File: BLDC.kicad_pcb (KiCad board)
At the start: 4 copper layers, 60 x 60 mm, 122 parts, among them J1 43650-0510, J2 436500313, J3 DNP, J4 43650-0510, U1 LMZ21700SIL, U12 MCP9808, U13 AS5047U, U17 INA250, U18 INA250, U19 INA250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

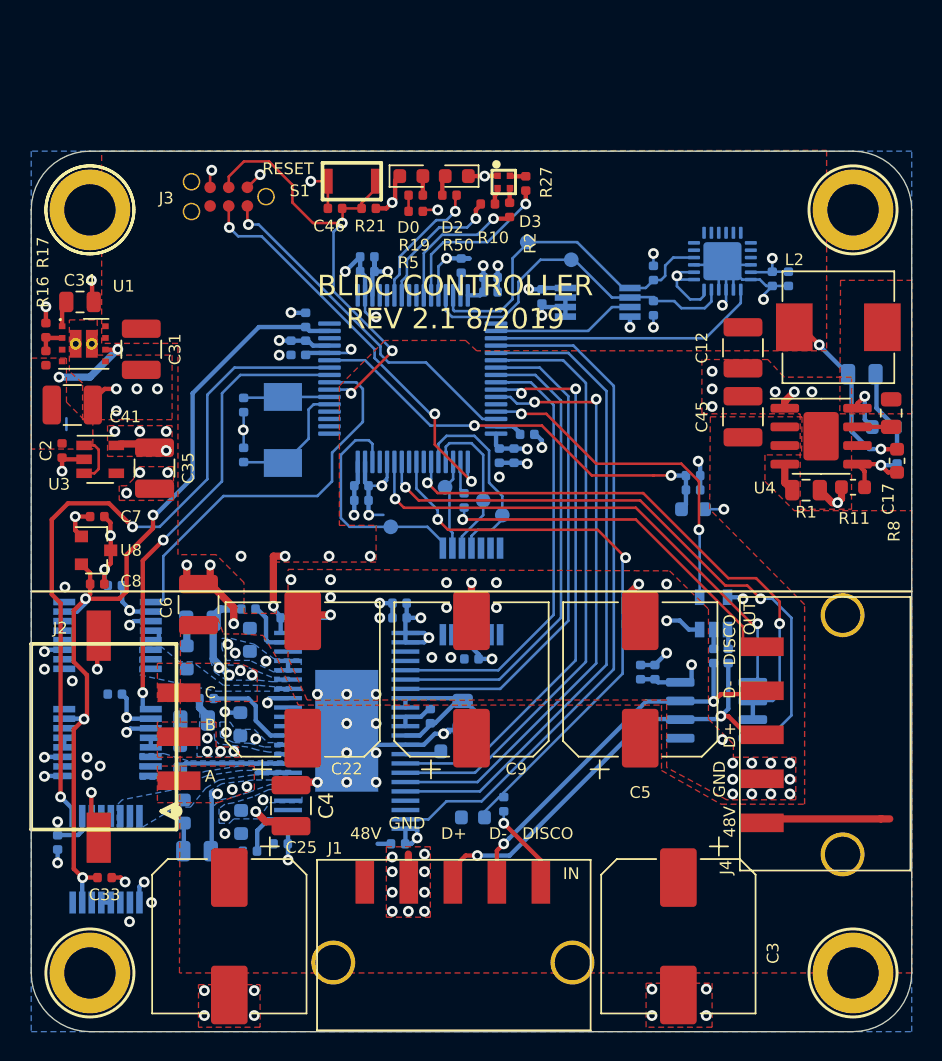
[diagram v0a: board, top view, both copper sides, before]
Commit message: more test points
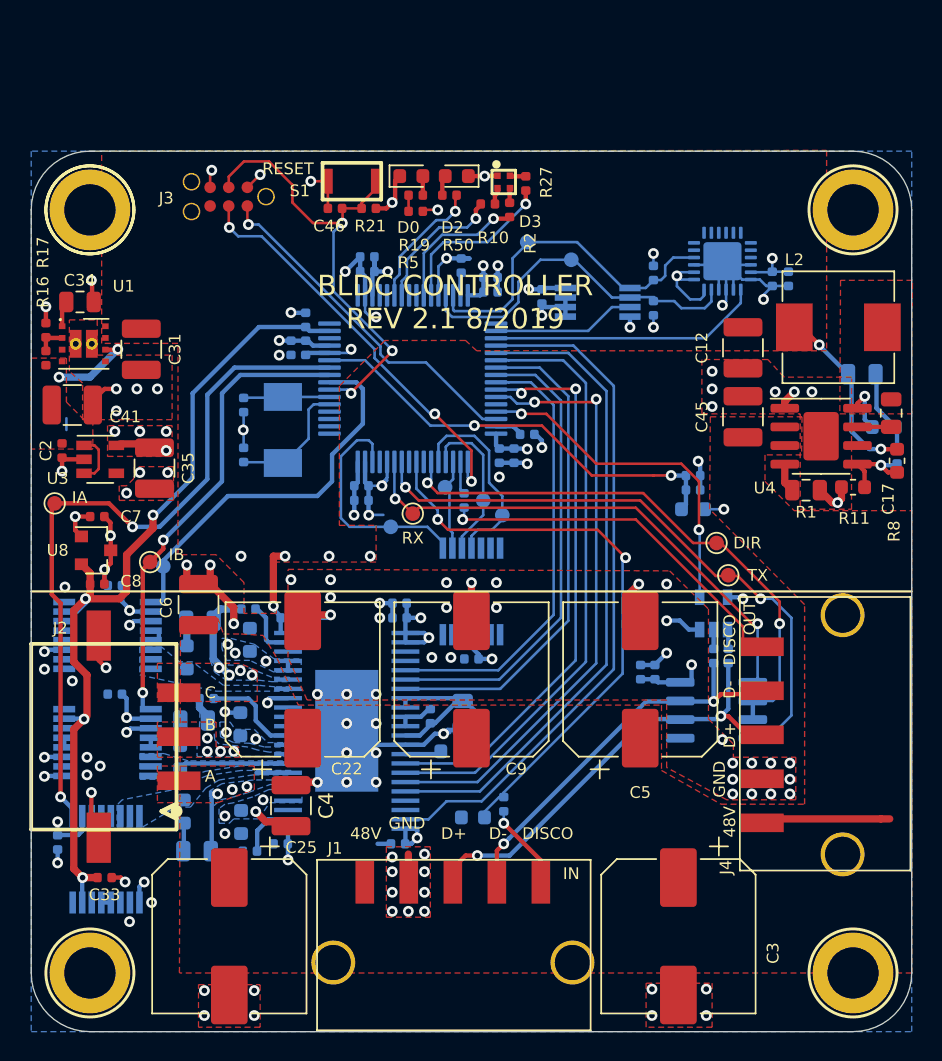
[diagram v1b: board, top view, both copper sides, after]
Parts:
- added TP10: TestPoint, TestPoint:TestPoint_Pad_D1.0mm, B.Cu at (127.5, 103.3)
- added TP11: TestPoint, TestPoint:TestPoint_Pad_D1.0mm, F.Cu at (120.1, 99.0)
- added TP12: TestPoint, TestPoint:TestPoint_Pad_D1.0mm, F.Cu at (126.6, 103.0)
- added TP7: TestPoint, TestPoint:TestPoint_Pad_D1.0mm, F.Cu at (166.0, 103.9)
- added TP8: TestPoint, TestPoint:TestPoint_Pad_D1.0mm, F.Cu at (165.2, 101.7)
- added TP9: TestPoint, TestPoint:TestPoint_Pad_D1.0mm, F.Cu at (144.5, 99.7)
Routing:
- net /ISENSE_A: track 48.7 -> 49.2 mm
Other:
- board text added: "DIR"
- board text added: "IA"
- board text added: "IB"
- board text added: "IC"
- board text added: "RX"
- board text added: "TX"

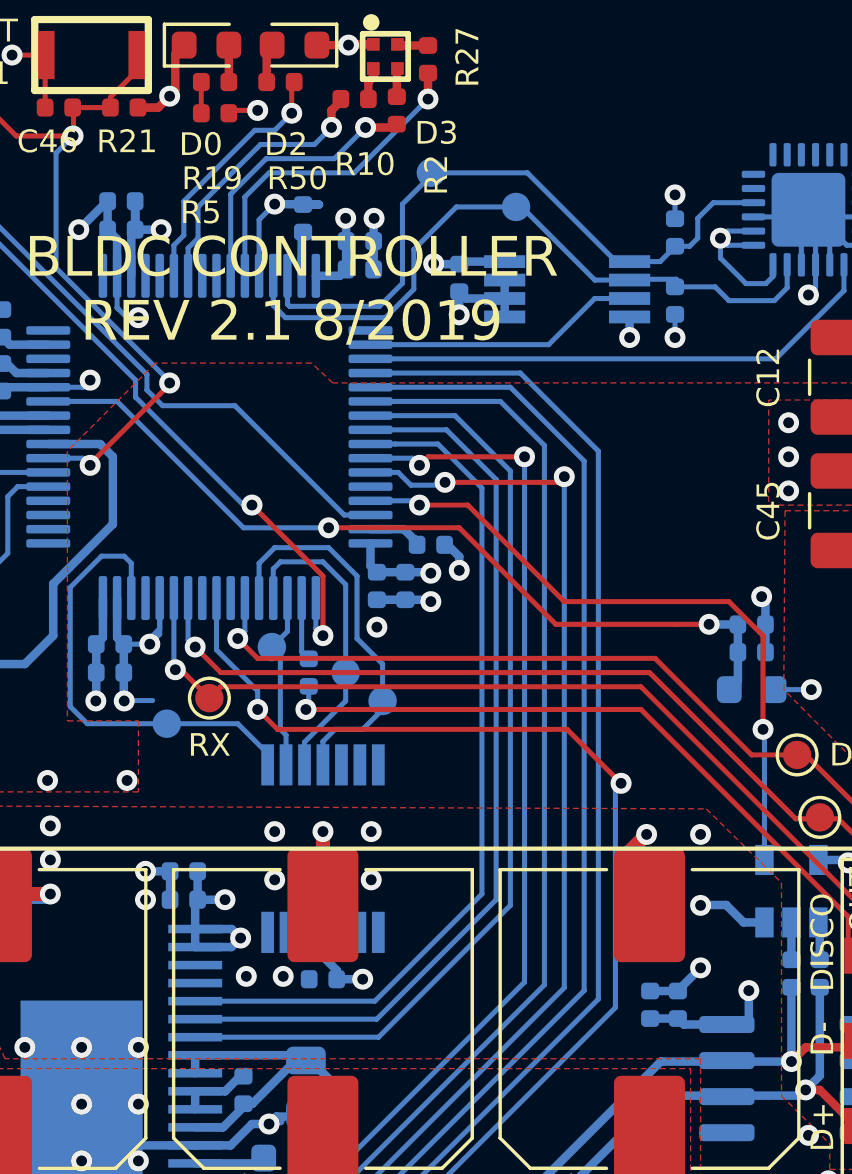
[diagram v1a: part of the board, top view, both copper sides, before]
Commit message: PWM test points
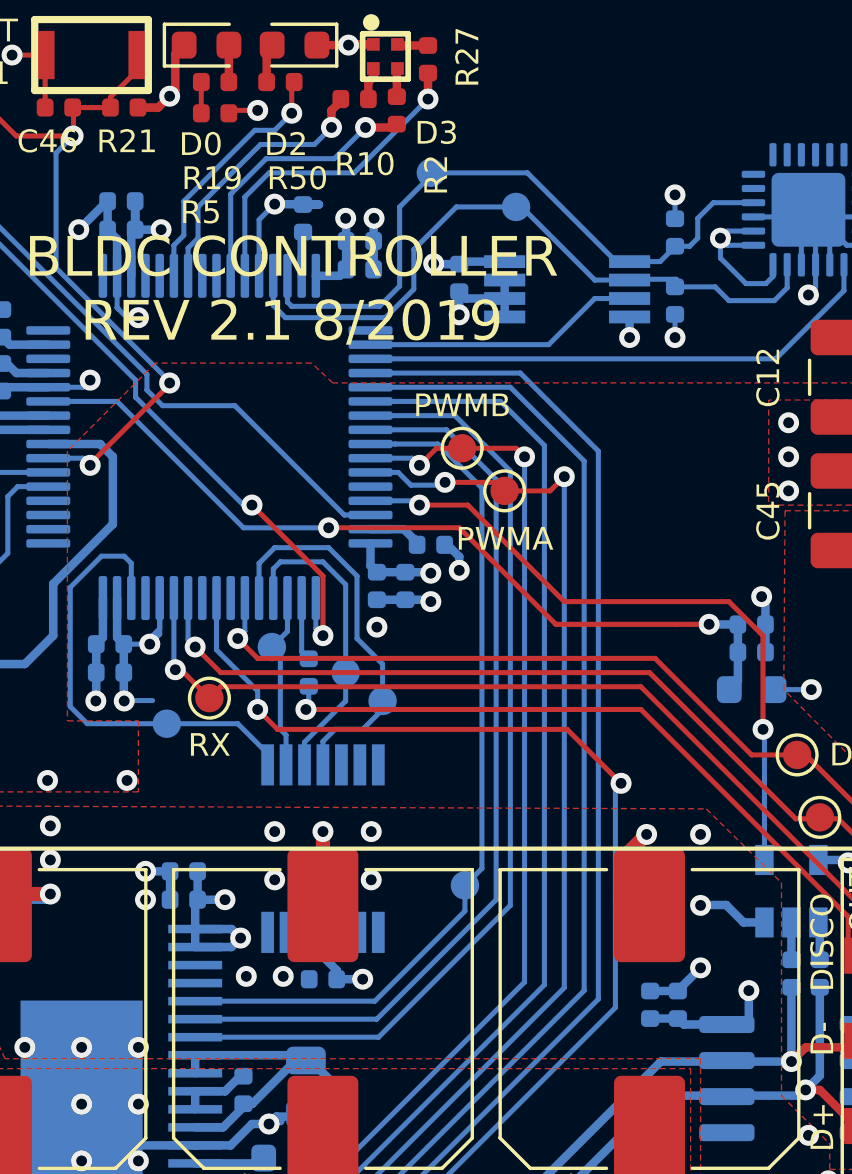
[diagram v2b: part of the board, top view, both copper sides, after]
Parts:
- added TP13: TestPoint, TestPoint:TestPoint_Pad_D1.0mm, F.Cu at (153.4, 90.9)
- added TP14: TestPoint, TestPoint:TestPoint_Pad_D1.0mm, F.Cu at (154.9, 92.4)
- added TP15: TestPoint, TestPoint:TestPoint_Pad_D1.0mm, B.Cu at (153.5, 106.3)
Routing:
- net /MOT_PWM_A: track 41.5 -> 42.0 mm
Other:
- board text added: "PWMA"
- board text added: "PWMB"
- board text added: "PWMC"

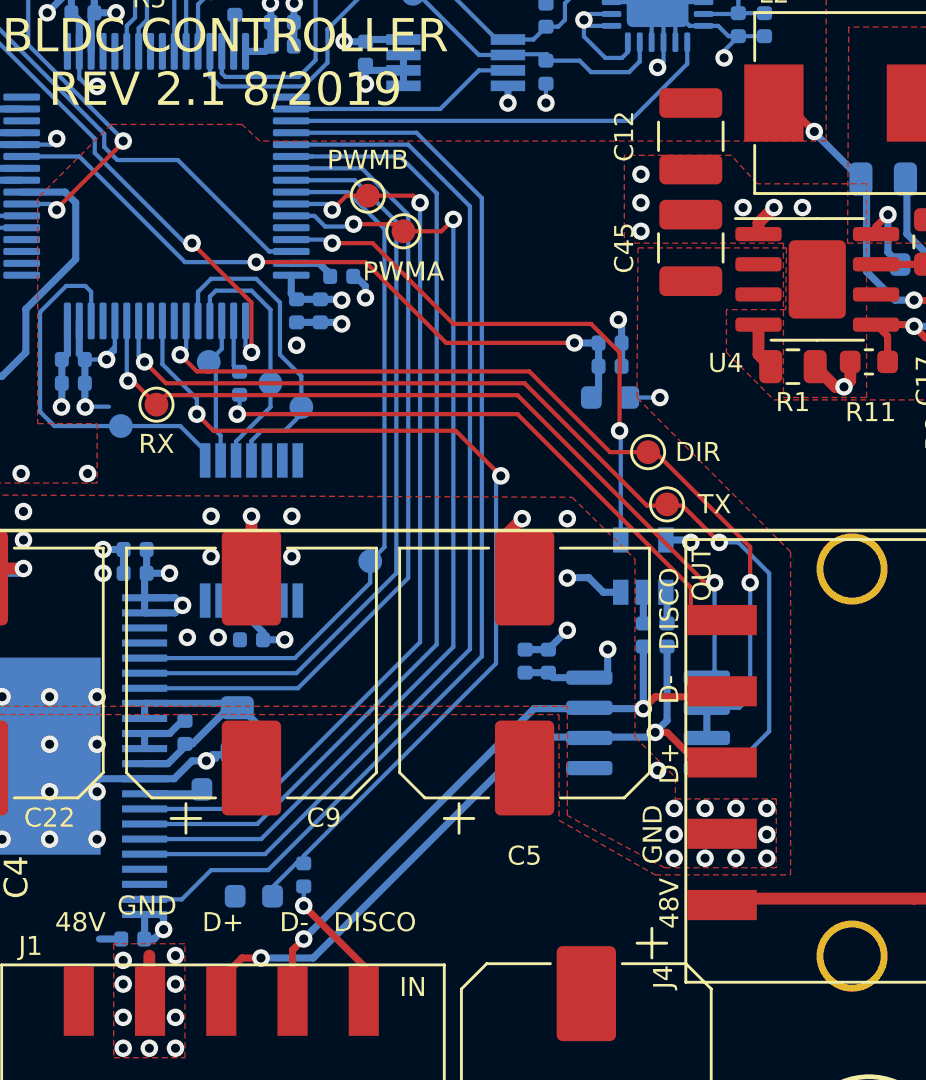
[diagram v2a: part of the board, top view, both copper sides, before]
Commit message: add TVS diodes to input and output disco bus connector pins
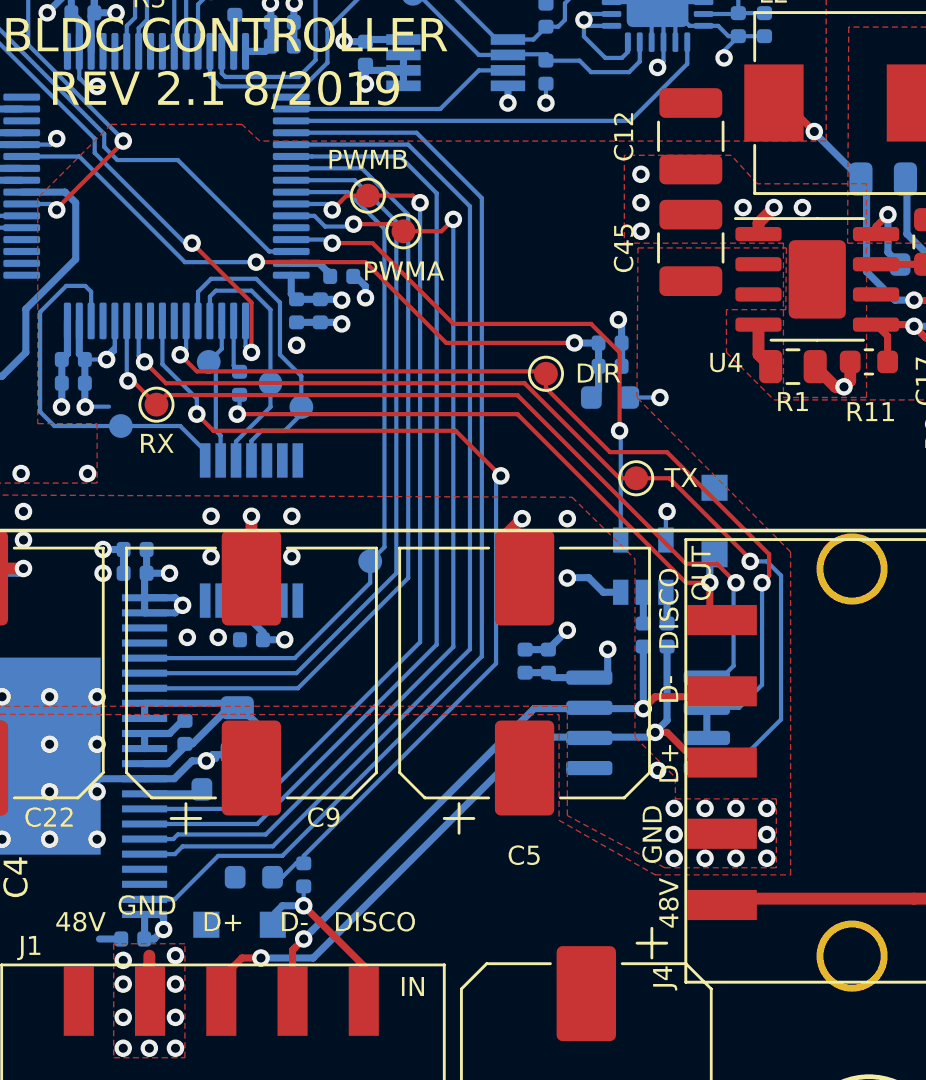
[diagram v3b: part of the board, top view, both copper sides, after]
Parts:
- added D1: SMF3.3, Diode_SMD:D_SOD-123F, B.Cu at (148.0, 121.6)
- added D4: SMF3.3, Diode_SMD:D_SOD-123F, B.Cu at (168.0, 104.6)
- moved TP8 5.42 mm to (160.9, 98.4)
- moved TP7 1.70 mm to (164.7, 102.8)
- moved R62 0.80 mm to (148.6, 119.6)
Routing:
- net Net-(D4-Pad1): track 26.5 -> 27.9 mm, vias 1 -> 2
- net Net-(D1-Pad1): track 5.88 -> 7.21 mm
- net /RS485_DIR: track 38.5 -> 39.8 mm
- net /UART_RX: track 35.8 -> 36.9 mm
- net /UART_TX: track 41.7 -> 42.4 mm
- net /DISCO_BUS_IN: track 40.3 -> 39.6 mm

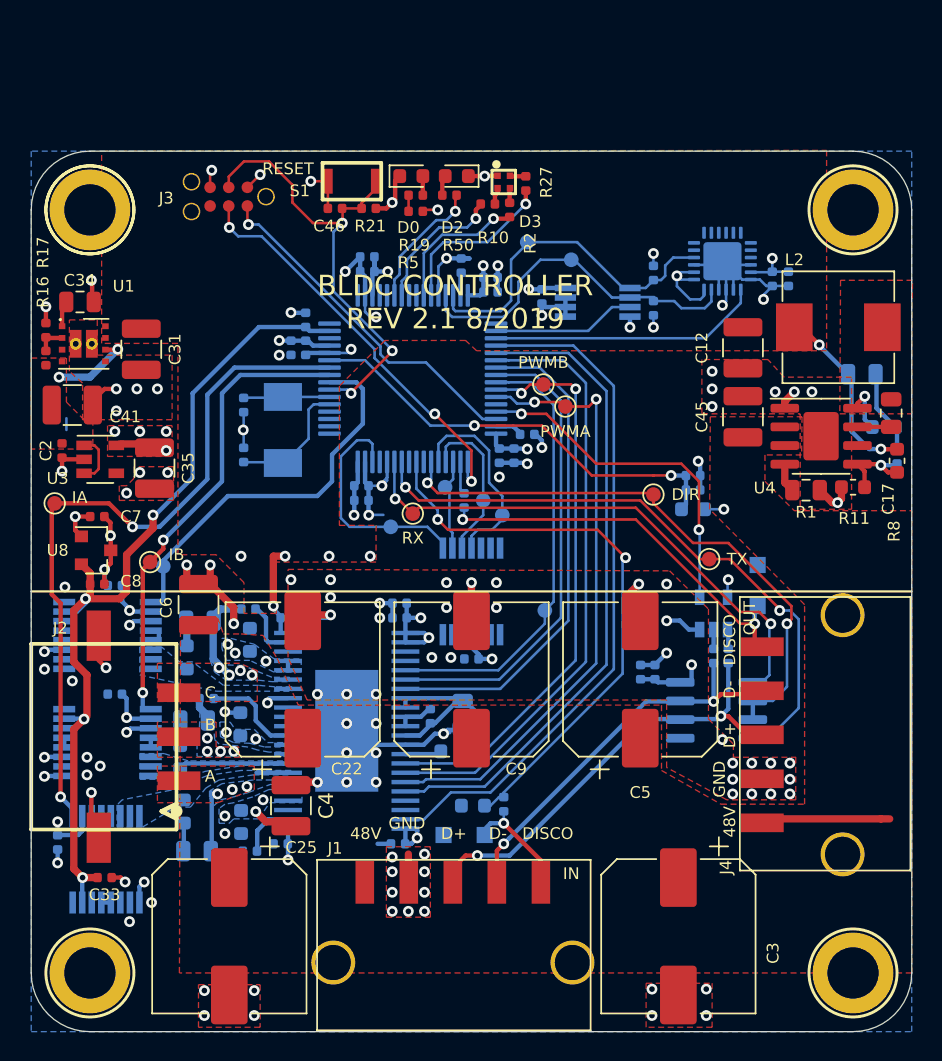
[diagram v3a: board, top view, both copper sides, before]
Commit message: clear out north edge of PCB for upcoming bonus header
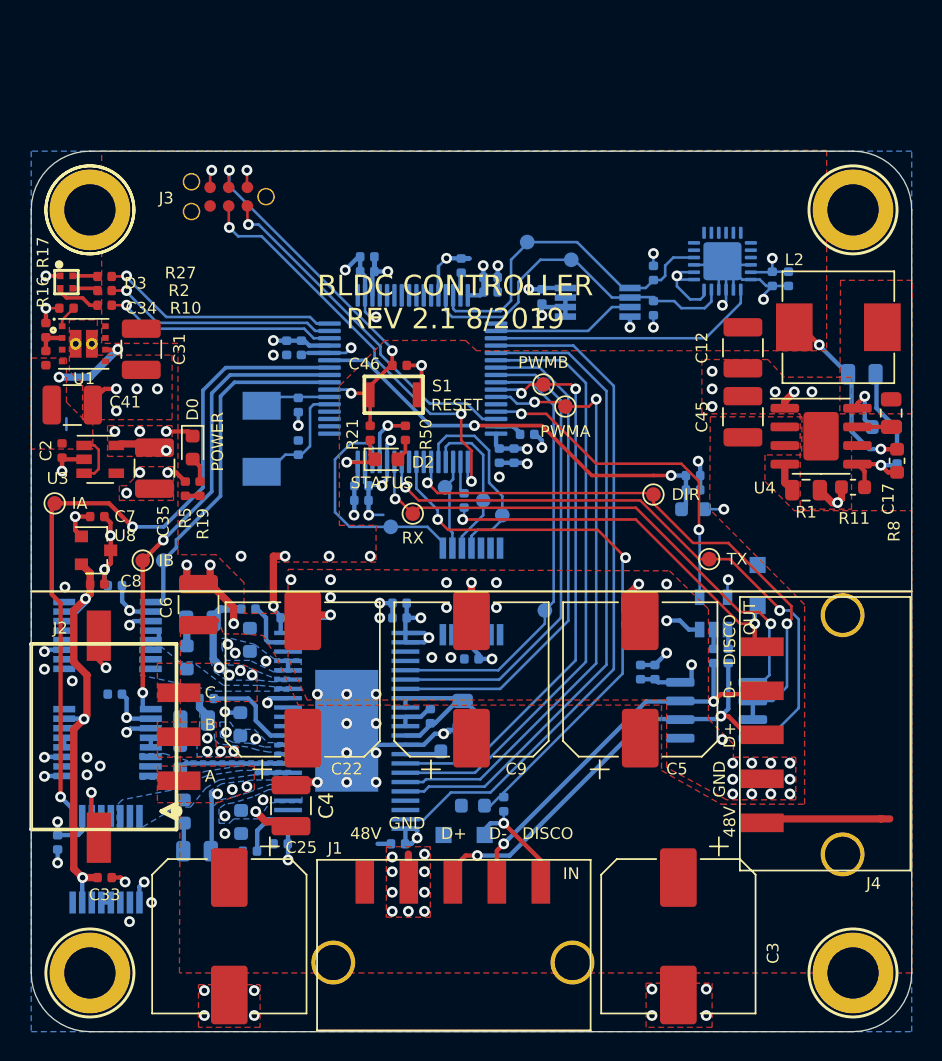
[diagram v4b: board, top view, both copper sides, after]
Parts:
- removed C37: 100n, Capacitor_SMD:C_0402_1005Metric
- C34: value 2n2 -> 3n3; footprint Capacitor_SMD:C_0805_2012Metric -> Capacitor_SMD:C_0402_1005Metric
- moved D3 30.6 mm to (120.9, 83.9)
- moved R27 29.4 mm to (123.5, 83.5), turned to 0 degrees
- moved R2 28.1 mm to (123.5, 84.5), turned to 0 degrees
- moved R10 27.0 mm to (123.5, 85.5), turned to 0 degrees
- moved R19 24.8 mm to (130.0, 98.0), turned to 270 degrees
- moved R5 24.6 mm to (129.0, 98.0), turned to 90 degrees
- moved D0 23.8 mm to (129.5, 95.2), turned to 270 degrees
- moved D2 19.9 mm to (142.7, 96.0), turned to 0 degrees
- moved R50 16.5 mm to (144.0, 94.2), turned to 90 degrees
- moved R21 15.3 mm to (141.6, 94.2), turned to 270 degrees
- moved S1 14.8 mm to (143.2, 91.6), turned to 180 degrees
- moved C46 11.6 mm to (143.6, 89.6), turned to 180 degrees
- moved C54 3.76 mm to (136.7, 95.2)
- moved C57 3.72 mm to (136.7, 92.3)
- moved X0 1.57 mm to (134.2, 94.6)
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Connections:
- U9 pad 14: Net-(U9-Pad14) -> /LED_G
- U9 pad 15: +1V2 -> /LED_B
- U9 pad 16: Net-(U9-Pad16) -> /LED_R
- U9 pad 22: /LED_STATUS -> Net-(U9-Pad22)
- U9 pad 23: /LED_G -> Net-(U9-Pad23)
- U9 pad 26: /LED_B -> Net-(U9-Pad26)
- U9 pad 27: /LED_R -> Net-(U9-Pad27)
- U9 pad 61: Net-(U9-Pad61) -> /LED_STATUS
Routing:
- net +1V2: track 58.9 -> 29.1 mm, vias 4 -> 3
- net /LED_B: track 9.75 -> 15.9 mm
- net /LED_G: track 9.57 -> 15.7 mm
- net /SWD_RESET: track 32.2 -> 26.9 mm
- net /LED_STATUS: track 8.99 -> 3.91 mm
- net /LED_R: track 11.6 -> 16.2 mm
- net Net-(C57-Pad2): track 6.22 -> 3.40 mm
- net /ISENSE_C: track 26.3 -> 23.5 mm
- net +3V3: track 63.4 -> 65.6 mm
- net Net-(D3-Pad4): track 1.17 -> 3.15 mm
- net Net-(C54-Pad2): track 9.75 -> 8.05 mm
- net GND: track 135.5 -> 134.3 mm, vias 120 -> 118
- net /SWD_SWCLK: track 28.2 -> 29.2 mm
- net Net-(D3-Pad3): track 1.00 -> 1.75 mm
- net Net-(D3-Pad2): track 1.09 -> 1.75 mm
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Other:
- board text added: "POWER"
- board text added: "STATUS"
